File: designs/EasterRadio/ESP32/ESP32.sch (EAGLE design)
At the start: 19 parts, among them IC1 ESP32-WROVER-E

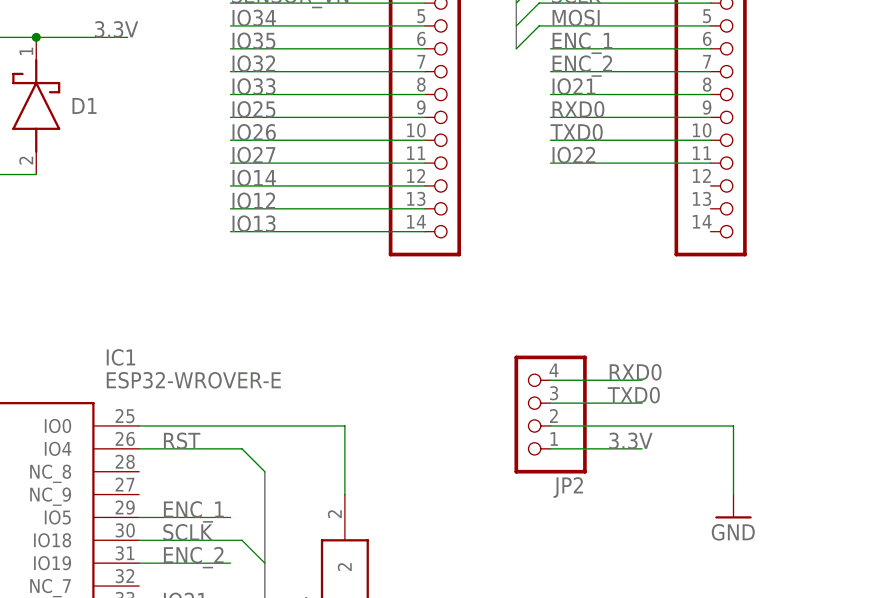
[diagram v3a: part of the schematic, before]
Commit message: added new design of radio parts added 3.3V mark
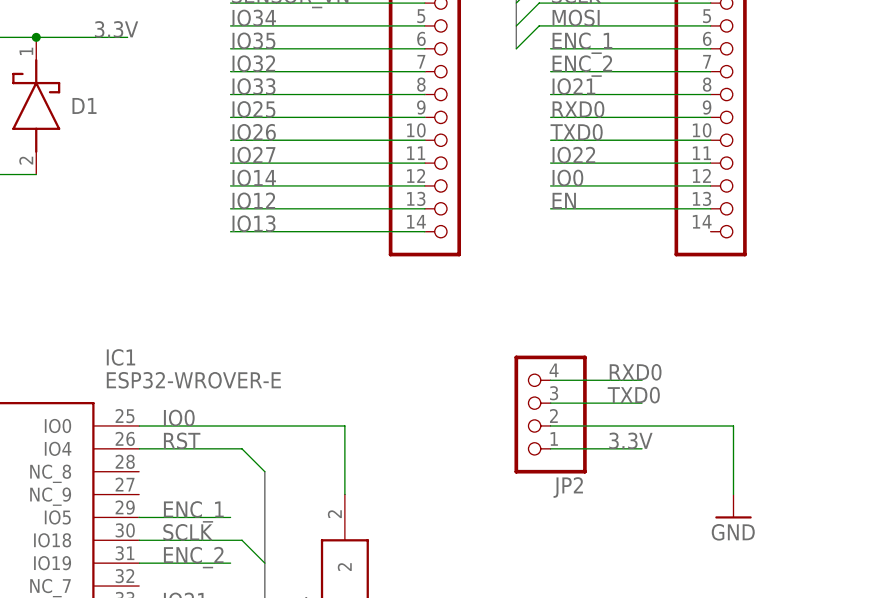
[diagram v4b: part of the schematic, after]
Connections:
- removed net IO1: IC1.IO0, S1.2
- new net IO0: IC1.IO0, JP4.12, S1.2
- net EN: now also JP4.13
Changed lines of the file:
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@@
 <setting verticaltext="up"/>
 </settings>
-<grid distance="50" unitdist="mil" unit="mil" style="lines" multiple="1" display="no" altdistance="0.01" altunitdist="inch" altunit="inch"/>
+<grid distance="0.05" unitdist="inch" unit="inch" style="lines" multiple="1" display="no" altdistance="0.01" altunitdist="inch" altunit="inch"/>
 <layers>
 <layer number="1" name="Top" color="4" fill="1" visible="no" active="no"/>
@@
 <pinref part="IC1" gate="G$1" pin="EN"/>
 </segment>
+<segment>
+<pinref part="JP4" gate="A" pin="13"/>
+<wire x1="171.45" y1="102.87" x2="153.67" y2="102.87" width="0.1524" layer="91"/>
+<label x="153.67" y="102.87" size="1.778" layer="95"/>
+</segment>
 </net>
 <net name="EN_1" class="1">
@@
 </segment>
 </net>
-<net name="IO1" class="1">
+<net name="IO0" class="1">
 <segment>
 <wire x1="107.95" y1="78.74" x2="130.81" y2="78.74" width="0.1524" layer="91" grouprefs="ESP32"/>
@@
 <pinref part="S1" gate="G$1" pin="2"/>
 <pinref part="IC1" gate="G$1" pin="IO0"/>
-</segment>
-</net>
+<label x="110.49" y="78.74" size="1.778" layer="95"/>
+</segment>
+<segment>
+<pinref part="JP4" gate="A" pin="12"/>
+<wire x1="171.45" y1="105.41" x2="153.67" y2="105.41" width="0.1524" layer="91"/>
+<label x="153.67" y="105.41" size="1.778" layer="95"/>
+</segment>
+</net>

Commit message: checked Mainboard and esp32
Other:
- note added: "Revision 1 02.04.21"
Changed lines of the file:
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@@
 <setting verticaltext="up"/>
 </settings>
-<grid distance="0.05" unitdist="inch" unit="inch" style="lines" multiple="1" display="no" altdistance="0.01" altunitdist="inch" altunit="inch"/>
+<grid distance="0.1" unitdist="inch" unit="inch" style="lines" multiple="1" display="no" altdistance="0.01" altunitdist="inch" altunit="inch"/>
 <layers>
 <layer number="1" name="Top" color="4" fill="1" visible="no" active="no"/>
@@
 <text x="0" y="158.75" size="5.08" layer="91">ESP32 (ESP32-Wrover-B)</text>
 <frame x1="0" y1="0" x2="215.9" y2="154.94" columns="8" rows="5" layer="91"/>
+<text x="86.36" y="157.48" size="1.778" layer="91">Revision 1 02.04.21</text>
 </plain>
 <instances>

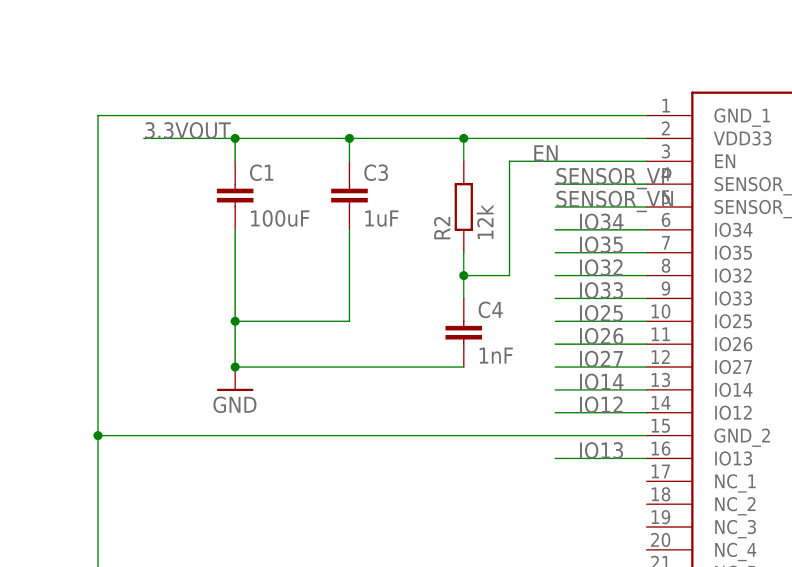
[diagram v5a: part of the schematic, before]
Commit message: minor changes to ESP32 values of resistor and capacitor
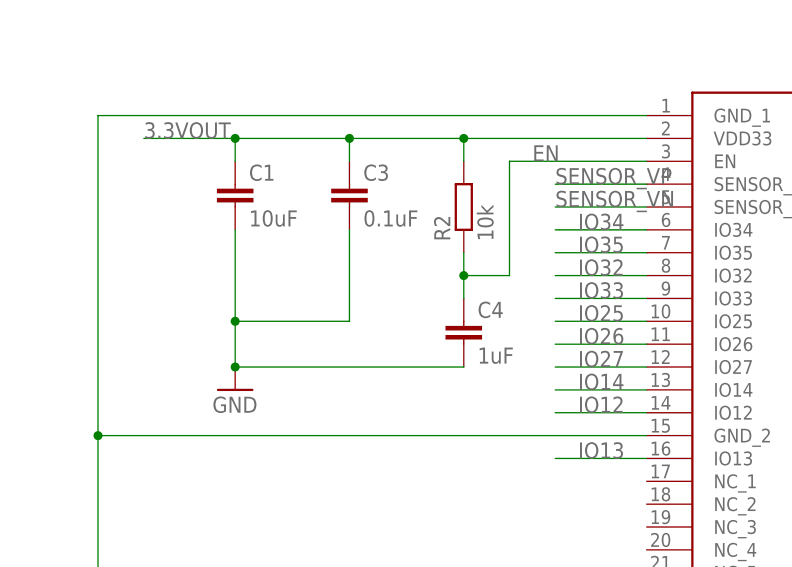
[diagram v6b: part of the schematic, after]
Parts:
- C1: value 100uF -> 10uF
- C3: value 1uF -> 0.1uF
- C4: value 1nF -> 1uF
- R2: value 12k -> 10k
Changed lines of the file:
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@@
 <part name="GND4" library="supply1" library_urn="urn:adsk.eagle:library:371" deviceset="GND" device=""/>
 <part name="GND5" library="supply1" library_urn="urn:adsk.eagle:library:371" deviceset="GND" device=""/>
-<part name="C1" library="CommonParts" deviceset="C-EU_1206" device="C1206" package3d_urn="urn:adsk.eagle:package:23618/2" value="100uF"/>
-<part name="C3" library="CommonParts" deviceset="C-EU_805" device="C0805" package3d_urn="urn:adsk.eagle:package:23617/2" value="1uF"/>
-<part name="R2" library="CommonParts" deviceset="R-EU_805" device="R0805" package3d_urn="urn:adsk.eagle:package:23553/2" value="12k"/>
-<part name="C4" library="CommonParts" deviceset="C-EU_805" device="C0805" package3d_urn="urn:adsk.eagle:package:23617/2" value="1nF"/>
+<part name="C1" library="CommonParts" deviceset="C-EU_1206" device="C1206" package3d_urn="urn:adsk.eagle:package:23618/2" value="10uF"/>
+<part name="C3" library="CommonParts" deviceset="C-EU_805" device="C0805" package3d_urn="urn:adsk.eagle:package:23617/2" value="0.1uF"/>
+<part name="R2" library="CommonParts" deviceset="R-EU_805" device="R0805" package3d_urn="urn:adsk.eagle:package:23553/2" value="10k"/>
+<part name="C4" library="CommonParts" deviceset="C-EU_805" device="C0805" package3d_urn="urn:adsk.eagle:package:23617/2" value="1uF"/>
 <part name="PS1" library="MouserUseful" deviceset="LP38693MPX-5.0_NOPB" device="" package3d_urn="urn:adsk.eagle:package:13422906/1"/>
 <part name="C2" library="rcl" library_urn="urn:adsk.eagle:library:334" deviceset="C-EU" device="C0805" package3d_urn="urn:adsk.eagle:package:23617/2"/>
